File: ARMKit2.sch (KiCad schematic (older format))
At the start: 36 parts, among them P1 CONN_01X06, P2 CONN_01X32, P3 CONN_01X32, P4 USB_B, U1 STM32F405RG, U2 LT1761, Y1 Crystal, Y2 Crystal

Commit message: Added VBAT to breakout header, cleaned up RES fp size, cleaned up silkscreen
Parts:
- R1, R2, R3, R4, R5: footprint Resistors_SMD:R_0805 -> Capacitors_SMD:C_0805
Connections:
- net GND: no longer P3.3 (P3)
- net VBAT: now also P3.3 (P3)
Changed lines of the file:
@@
 LIBS:contrib
 LIBS:valves
+LIBS:ARMKit2-cache
 EELAYER 25 0
 EELAYER END
@@
 F 0 "R1" V 5955 950 50  0000 C CNN
 F 1 "10k" V 5825 950 50  0000 C CNN
-F 2 "Resistors_SMD:R_0805" V 5805 950 30  0001 C CNN
+F 2 "Capacitors_SMD:C_0805" V 5805 950 30  0001 C CNN
 F 3 "" H 5875 950 30  0000 C CNN
 	1    5875 950
@@
 F 0 "R2" V 7355 4375 50  0000 C CNN
 F 1 "0" V 7225 4375 50  0000 C CNN
-F 2 "Resistors_SMD:R_0805" V 7205 4375 30  0001 C CNN
+F 2 "Capacitors_SMD:C_0805" V 7205 4375 30  0001 C CNN
 F 3 "" H 7275 4375 30  0000 C CNN
 	1    7275 4375
@@
 F 0 "R3" V 6580 1325 50  0000 C CNN
 F 1 "0" V 6450 1325 50  0000 C CNN
-F 2 "Resistors_SMD:R_0805" V 6430 1325 30  0001 C CNN
+F 2 "Capacitors_SMD:C_0805" V 6430 1325 30  0001 C CNN
 F 3 "" H 6500 1325 30  0000 C CNN
 	1    6500 1325
@@
 $Comp
 L GND #PWR013
-U 1 1 561DA544
-P 10675 3500
-F 0 "#PWR013" H 10675 3250 50  0001 C CNN
-F 1 "GND" H 10675 3350 50  0000 C CNN
-F 2 "" H 10675 3500 60  0000 C CNN
-F 3 "" H 10675 3500 60  0000 C CNN
-	1    10675 3500
-	0    1    1    0
-$EndComp
-$Comp
-L GND #PWR014
 U 1 1 561DA58E
 P 9450 3575
-F 0 "#PWR014" H 9450 3325 50  0001 C CNN
+F 0 "#PWR013" H 9450 3325 50  0001 C CNN
 F 1 "GND" H 9450 3425 50  0000 C CNN
 F 2 "" H 9450 3575 60  0000 C CNN
@@
 $EndComp
 $Comp
-L GND #PWR015
+L GND #PWR014
 U 1 1 561DA5D8
 P 10400 3600
-F 0 "#PWR015" H 10400 3350 50  0001 C CNN
+F 0 "#PWR014" H 10400 3350 50  0001 C CNN
 F 1 "GND" H 10400 3450 50  0000 C CNN
 F 2 "" H 10400 3600 60  0000 C CNN
@@
 Wire Wire Line
 	9450 3575 9525 3575
-Wire Wire Line
-	10675 3500 10775 3500
 Wire Wire Line
 	10400 3600 10775 3600
@@
 	9100 6275 9525 6275
 $Comp
-L GND #PWR016
+L GND #PWR015
 U 1 1 561DC569
 P 9450 6375
-F 0 "#PWR016" H 9450 6125 50  0001 C CNN
+F 0 "#PWR015" H 9450 6125 50  0001 C CNN
 F 1 "GND" H 9450 6225 50  0000 C CNN
 F 2 "" H 9450 6375 60  0000 C CNN
@@
 	10400 6000 10775 6000
 $Comp
-L GND #PWR017
+L GND #PWR016
 U 1 1 561DE647
 P 10425 6400
-F 0 "#PWR017" H 10425 6150 50  0001 C CNN
+F 0 "#PWR016" H 10425 6150 50  0001 C CNN
 F 1 "GND" H 10425 6250 50  0000 C CNN
 F 2 "" H 10425 6400 60  0000 C CNN
@@
 	10700 6100 10775 6100
 $Comp
-L GND #PWR018
+L GND #PWR017
 U 1 1 561DEBB6
 P 10425 6200
-F 0 "#PWR018" H 10425 5950 50  0001 C CNN
+F 0 "#PWR017" H 10425 5950 50  0001 C CNN
 F 1 "GND" H 10425 6050 50  0000 C CNN
 F 2 "" H 10425 6200 60  0000 C CNN
@@
 	10425 6200 10775 6200
 $Comp
-L GND #PWR019
+L GND #PWR018
 U 1 1 561DEBF5
 P 10725 6300
-F 0 "#PWR019" H 10725 6050 50  0001 C CNN
+F 0 "#PWR018" H 10725 6050 50  0001 C CNN
 F 1 "GND" H 10725 6150 50  0000 C CNN
 F 2 "" H 10725 6300 60  0000 C CNN
@@
 Connection ~ 8950 1550
 $Comp
-L GND #PWR020
+L GND #PWR019
 U 1 1 561DFB01
 P 8950 1700
-F 0 "#PWR020" H 8950 1450 50  0001 C CNN
+F 0 "#PWR019" H 8950 1450 50  0001 C CNN
 F 1 "GND" H 8950 1550 50  0000 C CNN
 F 2 "" H 8950 1700 60  0000 C CNN
@@
 Connection ~ 9525 1550
 $Comp
-L GND #PWR021
+L GND #PWR020
 U 1 1 561DFB8E
 P 9525 1700
-F 0 "#PWR021" H 9525 1450 50  0001 C CNN
+F 0 "#PWR020" H 9525 1450 50  0001 C CNN
 F 1 "GND" H 9525 1550 50  0000 C CNN
 F 2 "" H 9525 1700 60  0000 C CNN
@@
 Connection ~ 10125 1550
 $Comp
-L GND #PWR022
+L GND #PWR021
 U 1 1 561DFCC5
 P 10125 1700
-F 0 "#PWR022" H 10125 1450 50  0001 C CNN
+F 0 "#PWR021" H 10125 1450 50  0001 C CNN
 F 1 "GND" H 10125 1550 50  0000 C CNN
 F 2 "" H 10125 1700 60  0000 C CNN
@@
 Connection ~ 10700 1550
 $Comp
-L GND #PWR023
+L GND #PWR022
 U 1 1 561DFCE2
 P 10700 1700
-F 0 "#PWR023" H 10700 1450 50  0001 C CNN
+F 0 "#PWR022" H 10700 1450 50  0001 C CNN
 F 1 "GND" H 10700 1550 50  0000 C CNN
 F 2 "" H 10700 1700 60  0000 C CNN
@@
 	6775 2700 6650 2700
 Wire Wire Line
-	6650 2300 6650 2700
+	6650 2700 6650 2300
 Wire Wire Line
 	6275 2300 6775 2300
@@
 Connection ~ 6650 2300
 $Comp
-L GND #PWR024
+L GND #PWR023
 U 1 1 561F7AB6
 P 7375 3125
-F 0 "#PWR024" H 7375 2875 50  0001 C CNN
+F 0 "#PWR023" H 7375 2875 50  0001 C CNN
 F 1 "GND" H 7375 2975 50  0000 C CNN
 F 2 "" H 7375 3125 60  0000 C CNN
@@
 	7375 3125 7375 3000
 $Comp
-L GND #PWR025
+L GND #PWR024
 U 1 1 561F7AFD
 P 8475 2800
-F 0 "#PWR025" H 8475 2550 50  0001 C CNN
+F 0 "#PWR024" H 8475 2550 50  0001 C CNN
 F 1 "GND" H 8475 2650 50  0000 C CNN
 F 2 "" H 8475 2800 60  0000 C CNN
@@
 	8475 2800 8475 2675
 $Comp
-L GND #PWR026
+L GND #PWR025
 U 1 1 561F7B44
 P 6400 2800
-F 0 "#PWR026" H 6400 2550 50  0001 C CNN
+F 0 "#PWR025" H 6400 2550 50  0001 C CNN
 F 1 "GND" H 6400 2650 50  0000 C CNN
 F 2 "" H 6400 2800 60  0000 C CNN
@@
 F 0 "R4" V 6305 4825 50  0000 C CNN
 F 1 "470" V 6175 4825 50  0000 C CNN
-F 2 "Resistors_SMD:R_0805" V 6155 4825 30  0001 C CNN
+F 2 "Capacitors_SMD:C_0805" V 6155 4825 30  0001 C CNN
 F 3 "" H 6225 4825 30  0000 C CNN
 	1    6225 4825
@@
 	6225 4975 6225 5025
 $Comp
-L GND #PWR027
+L GND #PWR026
 U 1 1 561FA330
 P 6225 5025
-F 0 "#PWR027" H 6225 4775 50  0001 C CNN
+F 0 "#PWR026" H 6225 4775 50  0001 C CNN
 F 1 "GND" H 6225 4875 50  0000 C CNN
 F 2 "" H 6225 5025 60  0000 C CNN
@@
 VDD1
 $Comp
-L GND #PWR028
+L GND #PWR027
 U 1 1 56281D50
 P 6375 6300
-F 0 "#PWR028" H 6375 6050 50  0001 C CNN
+F 0 "#PWR027" H 6375 6050 50  0001 C CNN
 F 1 "GND" H 6375 6150 50  0000 C CNN
 F 2 "" H 6375 6300 60  0000 C CNN
@@
 	6675 5675 6675 5750
 $Comp
-L GND #PWR029
+L GND #PWR028
 U 1 1 5629398F
 P 6075 6800
-F 0 "#PWR029" H 6075 6550 50  0001 C CNN
+F 0 "#PWR028" H 6075 6550 50  0001 C CNN
 F 1 "GND" H 6075 6650 50  0000 C CNN
 F 2 "" H 6075 6800 60  0000 C CNN
@@
 F 0 "R5" V 5980 4825 50  0000 C CNN
 F 1 "470" V 5850 4825 50  0000 C CNN
-F 2 "Resistors_SMD:R_0805" V 5830 4825 30  0001 C CNN
+F 2 "Capacitors_SMD:C_0805" V 5830 4825 30  0001 C CNN
 F 3 "" H 5900 4825 30  0000 C CNN
 	1    5900 4825
@@
 	5900 4975 5900 5025
 $Comp
-L GND #PWR030
+L GND #PWR029
 U 1 1 562941C7
 P 5900 5025
-F 0 "#PWR030" H 5900 4775 50  0001 C CNN
+F 0 "#PWR029" H 5900 4775 50  0001 C CNN
 F 1 "GND" H 5900 4875 50  0000 C CNN
 F 2 "" H 5900 5025 60  0000 C CNN
@@
 Text GLabel 6225 4100 1    60   Input ~ 0
 PC8
+Wire Wire Line
+	10775 3500 10675 3500
+Text GLabel 10675 3500 0    60   Input ~ 0
+VBAT
 $EndSCHEMATC

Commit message: Moved USB to PA11/PA12
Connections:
- net PA11: now also P4.2 (D-)
- net PA12: now also P4.3 (D+)
- net PB14: no longer P4.2 (D-)
- net PB15: no longer P4.3 (D+)
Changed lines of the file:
@@
 	-1   0    0    1
 $EndComp
-Text GLabel 6475 5975 1    60   Input ~ 0
-PB15
-Text GLabel 6575 6350 1    60   Input ~ 0
-PB14
 Wire Wire Line
 	6575 6350 6575 6400
@@
 Text GLabel 10675 3500 0    60   Input ~ 0
 VBAT
+Text GLabel 6575 6350 1    60   Input ~ 0
+PA11
+Text GLabel 6475 5975 1    60   Input ~ 0
+PA12
 $EndSCHEMATC

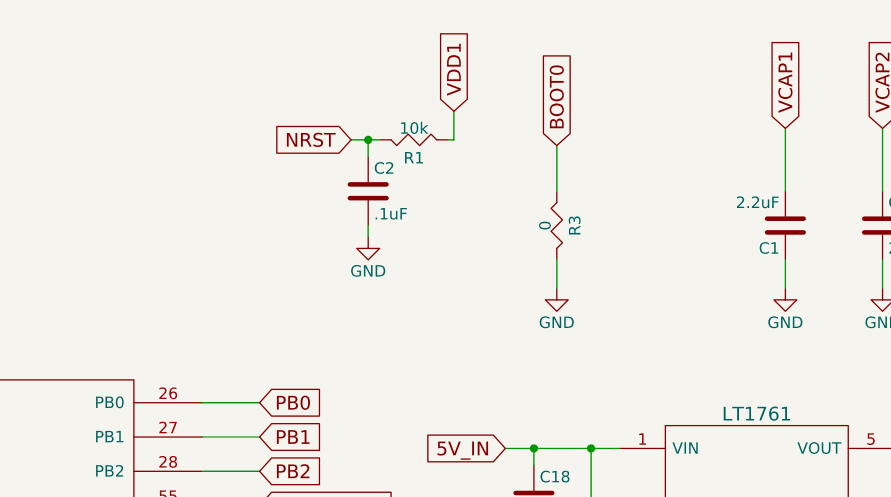
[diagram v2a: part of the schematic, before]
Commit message: Added BOOT and RESET buttons, much re-routing
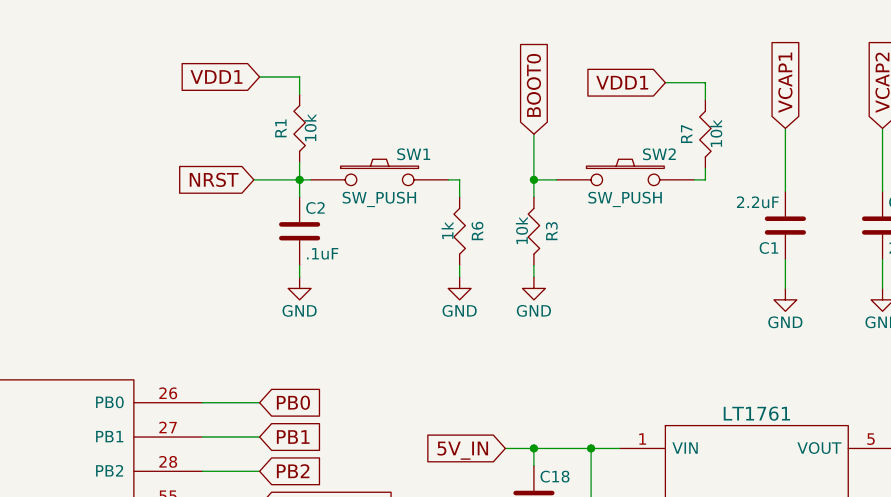
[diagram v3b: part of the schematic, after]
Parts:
- added R6: 1k, Capacitors_SMD:C_0805, symbol R
- added R7: 10k, Capacitors_SMD:C_0805, symbol R
- added SW1, SW2: SW_PUSH, Buttons_Switches_SMD:SW_SPST_FSMSM, symbol SW_PUSH
- R3: value 0 -> 10k
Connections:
- net BOOT0: now also SW2.1
- net GND: now also R6.2
- net NRST: now also R1.1, SW1.1; no longer R1.2
- net VDD1: now also R1.2, R7.2; no longer R1.1
- new net: R6.1, SW1.2
- new net: R7.1, SW2.2
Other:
- moved on the sheet: C2, R1, R3
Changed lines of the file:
@@
 Text GLabel 1100 2500 0    60   Input ~ 0
 NRST
-Text GLabel 5600 950  0    60   Input ~ 0
+Text GLabel 5175 1125 0    60   Input ~ 0
 NRST
 $Comp
 L R R1
 U 1 1 561C7DBD
-P 5875 950
-F 0 "R1" V 5955 950 50  0000 C CNN
-F 1 "10k" V 5825 950 50  0000 C CNN
-F 2 "Capacitors_SMD:C_0805" V 5805 950 30  0001 C CNN
-F 3 "" H 5875 950 30  0000 C CNN
-	1    5875 950
-	0    1    1    0
-$EndComp
-Wire Wire Line
-	6025 950  6050 950
-Wire Wire Line
-	6050 950  6050 825
-Wire Wire Line
-	5600 950  5725 950
+P 5375 900
+F 0 "R1" V 5455 900 50  0000 C CNN
+F 1 "10k" V 5325 900 50  0000 C CNN
+F 2 "Capacitors_SMD:C_0805" V 5305 900 30  0001 C CNN
+F 3 "" H 5375 900 30  0000 C CNN
+	1    5375 900
+	-1   0    0    1
+$EndComp
+Wire Wire Line
+	5375 1050 5375 1200
 Wire Wire Line
 	1300 2750 1100 2750
@@
 L C C2
 U 1 1 561CB51F
-P 5675 1175
-F 0 "C2" H 5700 1275 50  0000 L CNN
-F 1 ".1uF" H 5700 1075 50  0000 L CNN
-F 2 "Capacitors_SMD:C_0805" H 5713 1025 30  0001 C CNN
-F 3 "" H 5675 1175 60  0000 C CNN
-	1    5675 1175
+P 5375 1350
+F 0 "C2" H 5400 1450 50  0000 L CNN
+F 1 ".1uF" H 5400 1250 50  0000 L CNN
+F 2 "Capacitors_SMD:C_0805" H 5413 1200 30  0001 C CNN
+F 3 "" H 5375 1350 60  0000 C CNN
+	1    5375 1350
 	1    0    0    -1
 $EndComp
@@
 L GND #PWR09
 U 1 1 561CB6CC
-P 5675 1375
-F 0 "#PWR09" H 5675 1125 50  0001 C CNN
-F 1 "GND" H 5675 1225 50  0000 C CNN
-F 2 "" H 5675 1375 60  0000 C CNN
-F 3 "" H 5675 1375 60  0000 C CNN
-	1    5675 1375
-	1    0    0    -1
-$EndComp
-Wire Wire Line
-	5675 1325 5675 1375
-Wire Wire Line
-	5675 1025 5675 950
-Connection ~ 5675 950
-Wire Wire Line
-	6500 1175 6500 975
-Text GLabel 6500 975  1    60   Input ~ 0
+P 6075 1550
+F 0 "#PWR09" H 6075 1300 50  0001 C CNN
+F 1 "GND" H 6075 1400 50  0000 C CNN
+F 2 "" H 6075 1550 60  0000 C CNN
+F 3 "" H 6075 1550 60  0000 C CNN
+	1    6075 1550
+	1    0    0    -1
+$EndComp
+Wire Wire Line
+	6075 1500 6075 1550
+Wire Wire Line
+	6400 925  6400 1200
+Text GLabel 6400 925  1    60   Input ~ 0
 BOOT0
 $Comp
 L R R3
 U 1 1 561CCC5F
-P 6500 1325
-F 0 "R3" V 6580 1325 50  0000 C CNN
-F 1 "0" V 6450 1325 50  0000 C CNN
-F 2 "Capacitors_SMD:C_0805" V 6430 1325 30  0001 C CNN
-F 3 "" H 6500 1325 30  0000 C CNN
-	1    6500 1325
+P 6400 1350
+F 0 "R3" V 6480 1350 50  0000 C CNN
+F 1 "10k" V 6350 1350 50  0000 C CNN
+F 2 "Capacitors_SMD:C_0805" V 6330 1350 30  0001 C CNN
+F 3 "" H 6400 1350 30  0000 C CNN
+	1    6400 1350
 	1    0    0    -1
 $EndComp
@@
 L GND #PWR010
 U 1 1 561CCCB8
-P 6500 1600
-F 0 "#PWR010" H 6500 1350 50  0001 C CNN
-F 1 "GND" H 6500 1450 50  0000 C CNN
-F 2 "" H 6500 1600 60  0000 C CNN
-F 3 "" H 6500 1600 60  0000 C CNN
-	1    6500 1600
-	1    0    0    -1
-$EndComp
-Wire Wire Line
-	6500 1600 6500 1475
+P 6400 1550
+F 0 "#PWR010" H 6400 1300 50  0001 C CNN
+F 1 "GND" H 6400 1400 50  0000 C CNN
+F 2 "" H 6400 1550 60  0000 C CNN
+F 3 "" H 6400 1550 60  0000 C CNN
+	1    6400 1550
+	1    0    0    -1
+$EndComp
+Wire Wire Line
+	6400 1550 6400 1500
 Wire Wire Line
 	1300 3200 1100 3200
@@
 Text GLabel 8175 5600 0    60   Input ~ 0
 VDD1
-Text GLabel 6050 825  1    60   Input ~ 0
+Text GLabel 5200 675  0    60   Input ~ 0
 VDD1
 $Comp
@@
 Text GLabel 6475 5975 1    60   Input ~ 0
 PA12
+$Comp
+L SW_PUSH SW1
+U 1 1 564AB04F
+P 5725 1125
+F 0 "SW1" H 5875 1235 50  0000 C CNN
+F 1 "SW_PUSH" H 5725 1045 50  0000 C CNN
+F 2 "Buttons_Switches_SMD:SW_SPST_FSMSM" H 5725 1125 60  0001 C CNN
+F 3 "" H 5725 1125 60  0000 C CNN
+	1    5725 1125
+	1    0    0    -1
+$EndComp
+Connection ~ 5375 1125
+$Comp
+L R R6
+U 1 1 564ABC53
+P 6075 1350
+F 0 "R6" V 6155 1350 50  0000 C CNN
+F 1 "1k" V 6025 1350 50  0000 C CNN
+F 2 "Capacitors_SMD:C_0805" V 6005 1350 30  0001 C CNN
+F 3 "" H 6075 1350 30  0000 C CNN
+	1    6075 1350
+	1    0    0    -1
+$EndComp
+Wire Wire Line
+	6025 1125 6075 1125
+Wire Wire Line
+	6075 1125 6075 1200
+$Comp
+L GND #PWR030
+U 1 1 564ABF58
+P 5375 1550
+F 0 "#PWR030" H 5375 1300 50  0001 C CNN
+F 1 "GND" H 5375 1400 50  0000 C CNN
+F 2 "" H 5375 1550 60  0000 C CNN
+F 3 "" H 5375 1550 60  0000 C CNN
+	1    5375 1550
+	1    0    0    -1
+$EndComp
+Wire Wire Line
+	5375 1500 5375 1550
+Wire Wire Line
+	5200 675  5375 675
+Wire Wire Line
+	5375 675  5375 750
+Wire Wire Line
+	5175 1125 5425 1125
+$Comp
+L SW_PUSH SW2
+U 1 1 564AE0CA
+P 6800 1125
+F 0 "SW2" H 6950 1235 50  0000 C CNN
+F 1 "SW_PUSH" H 6800 1045 50  0000 C CNN
+F 2 "Buttons_Switches_SMD:SW_SPST_FSMSM" H 6800 1125 60  0001 C CNN
+F 3 "" H 6800 1125 60  0000 C CNN
+	1    6800 1125
+	1    0    0    -1
+$EndComp
+$Comp
+L R R7
+U 1 1 564AE533
+P 7150 925
+F 0 "R7" V 7230 925 50  0000 C CNN
+F 1 "10k" V 7100 925 50  0000 C CNN
+F 2 "Capacitors_SMD:C_0805" V 7080 925 30  0001 C CNN
+F 3 "" H 7150 925 30  0000 C CNN
+	1    7150 925
+	-1   0    0    1
+$EndComp
+Text GLabel 6975 700  0    60   Input ~ 0
+VDD1
+Wire Wire Line
+	6975 700  7150 700
+Wire Wire Line
+	7150 700  7150 775
+Wire Wire Line
+	7100 1125 7150 1125
+Wire Wire Line
+	7150 1125 7150 1075
+Wire Wire Line
+	6500 1125 6400 1125
+Connection ~ 6400 1125
 $EndSCHEMATC

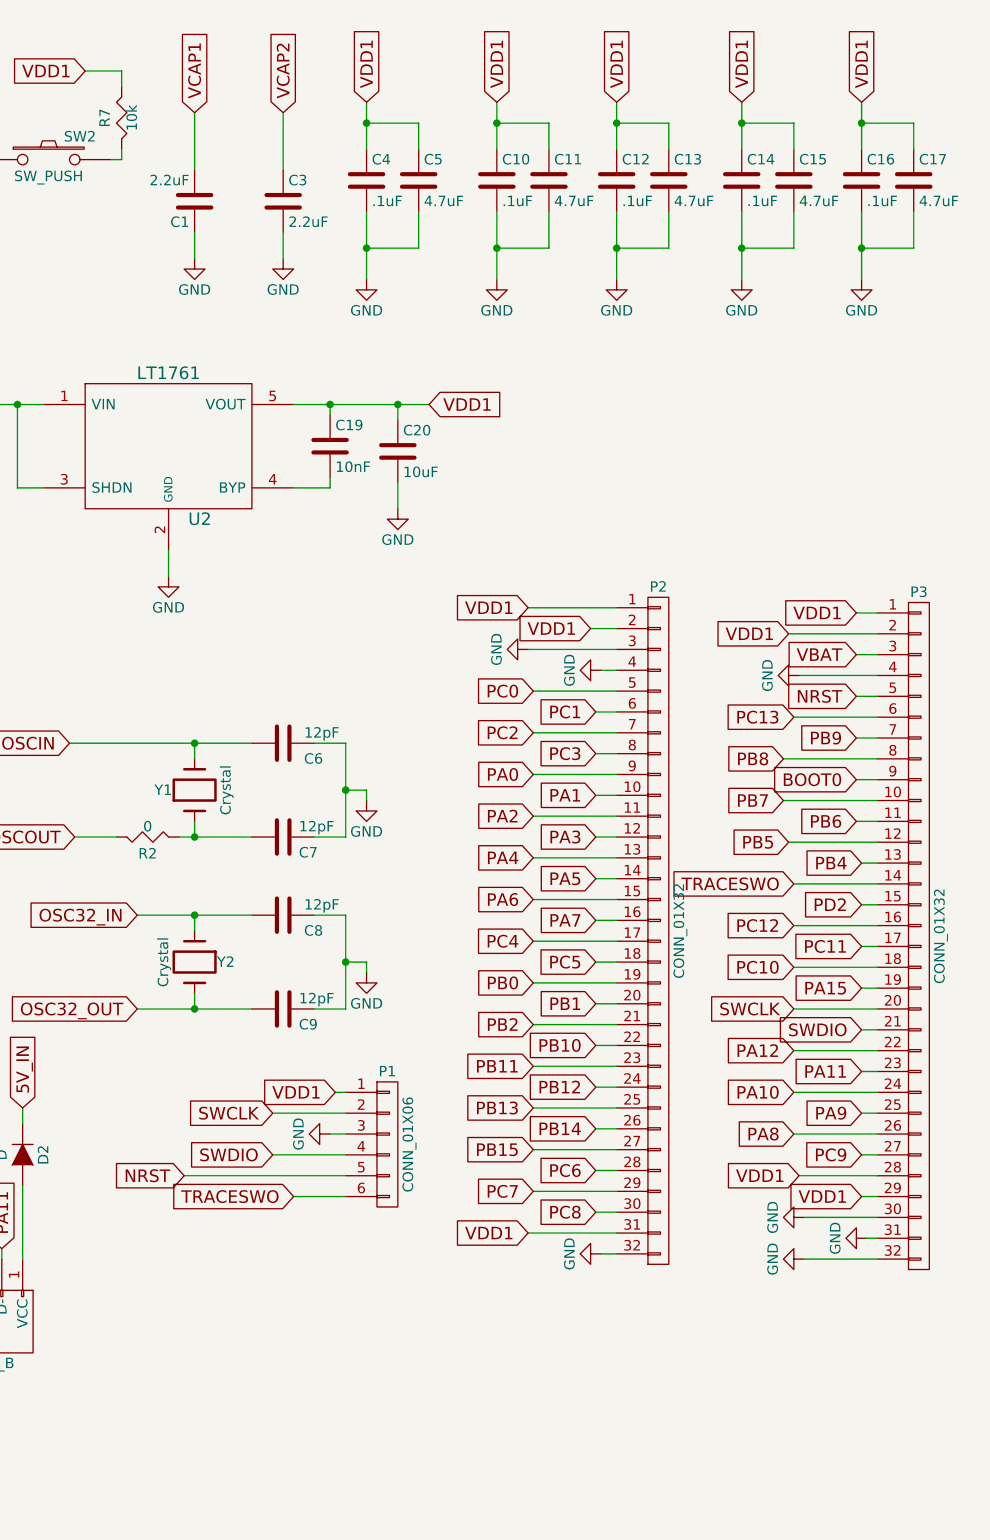
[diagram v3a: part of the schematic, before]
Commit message: Cleaned up some unused caps, added CC Attribution license
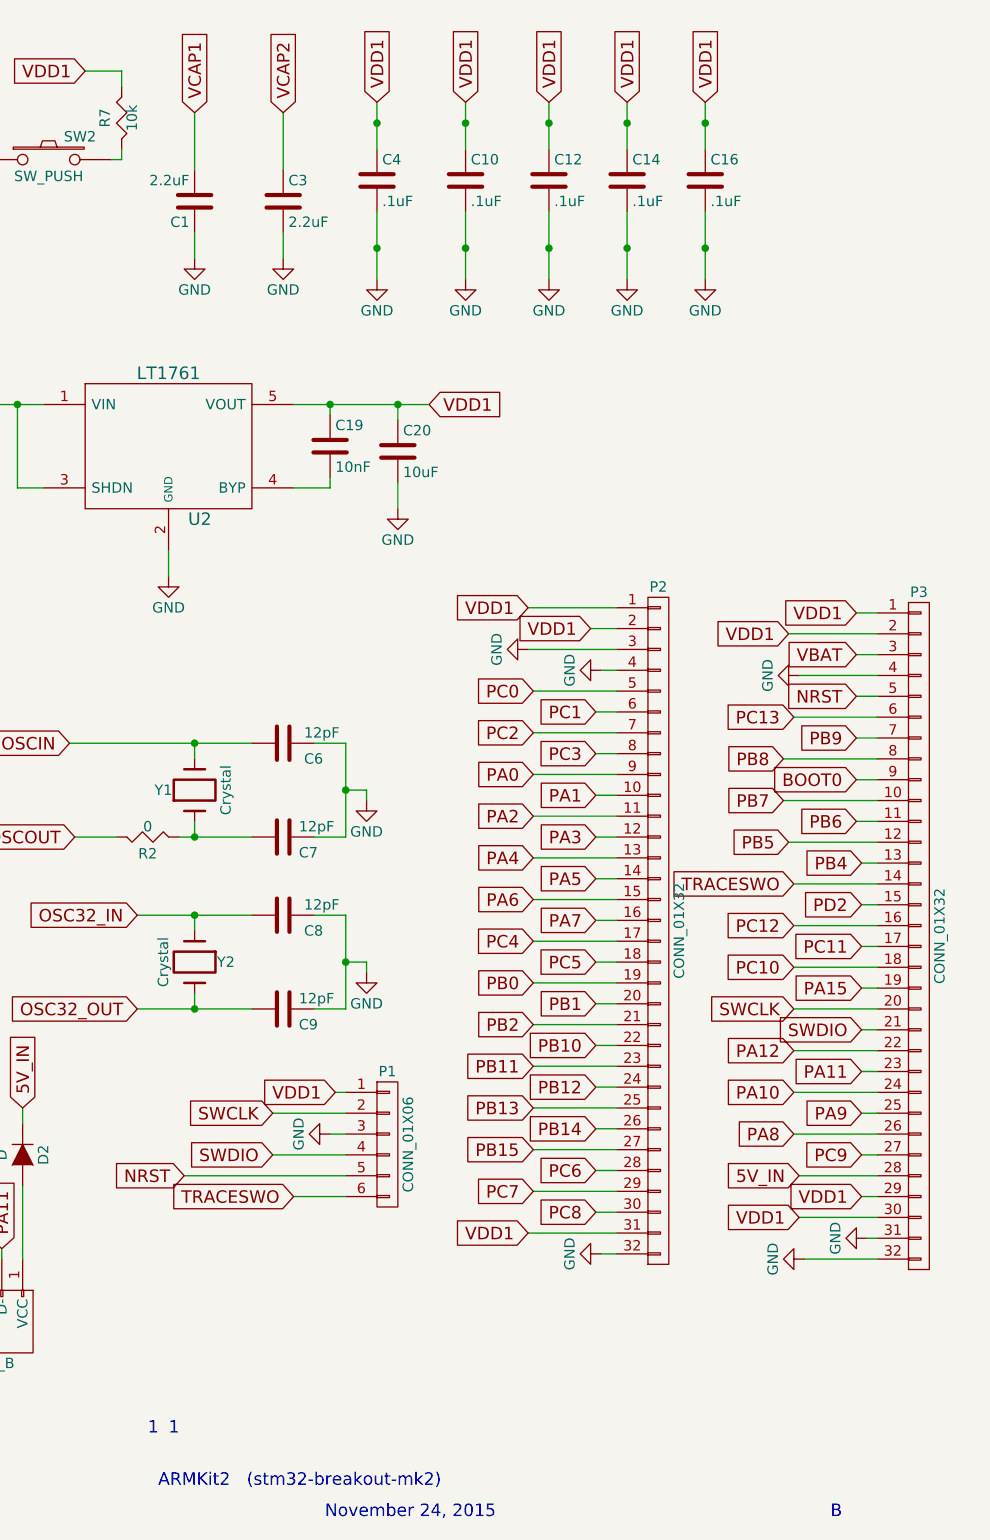
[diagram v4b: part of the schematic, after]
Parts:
- removed C11, C13, C15, C17, C5: 4.7uF, Capacitors_SMD:C_0805, symbol C
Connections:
- net 5V_IN: now also P3.28 (P28)
- net GND: no longer P3.30 (P30)
- net VDD1: now also P3.30 (P30); no longer P3.28 (P28)
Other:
- note added: "(stm32-breakout-mk2)"
- note added: "1"
- note added: "ARMKit2"
- note added: "B"
- note added: "November 24, 2015"
- moved on the sheet: C10, C12, C14, C16, C4

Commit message: More small changes to PCB, Schematic.  Gerber refresh
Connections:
- net PC13: now also P3.3 (P3); no longer P3.6 (P6)
- net VBAT: now also P3.6 (P6); no longer P3.3 (P3)
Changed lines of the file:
@@
 	10775 4800 10375 4800
 Wire Wire Line
-	10775 3800 10375 3800
+	10775 3500 10675 3500
 Text GLabel 9125 3675 0    60   Input ~ 0
 PC0
@@
 Text GLabel 10375 4800 0    60   Input ~ 0
 PC12
-Text GLabel 10375 3800 0    60   Input ~ 0
+Text GLabel 10675 3500 0    60   Input ~ 0
 PC13
 Wire Wire Line
@@
 	6775 2700 6650 2700
 Wire Wire Line
-	6650 2700 6650 2300
+	6650 2300 6650 2700
 Wire Wire Line
 	6275 2300 6775 2300
@@
 PC8
 Wire Wire Line
-	10775 3500 10675 3500
-Text GLabel 10675 3500 0    60   Input ~ 0
+	10775 3800 10350 3800
+Text GLabel 10350 3800 0    60   Input ~ 0
 VBAT
 Text GLabel 6575 6350 1    60   Input ~ 0
